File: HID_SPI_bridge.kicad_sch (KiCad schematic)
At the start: 10 parts, among them P1 USB_C_Plug_USB2.0, U1 STM32F042K4Tx

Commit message: [ADD](General) v1
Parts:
- added D2: D_Schottky, symbol Device:D_Schottky
- renumbered C6 to C122, C7 to C123, C5 to C124, C8 to C125, C4 to C126, C9 to C127, U1 to U2
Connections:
- net GND: no longer P1.S1 (SHIELD)
- net VBUS: now also D2.1 (K); no longer P1.A4 (VBUS), P1.A9 (VBUS), P1.B4 (VBUS), P1.B9 (VBUS)
- net NRST: now reaches C124.2, U2.4 (NRST)
- net CC: now reaches P1.A5 (CC), R10.2
- net SPI_SCK: now reaches U2.11 (PA5)
- net SPI_MISO: now reaches U2.12 (PA6)
- net SPI_MOSI: now reaches U2.13 (PA7)
- net USB-: now reaches P1.A7 (D-), U2.21 (PA11)
- net USB+: now reaches P1.A6 (D+), U2.22 (PA12)
- net SPI_CS: now reaches U2.6 (PA0)
- new net: D2.2 (A), P1.A4 (VBUS), P1.A9 (VBUS), P1.B4 (VBUS), P1.B9 (VBUS)
- no-connect marks 1 -> 20
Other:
- note added: "Microcontroller for USB interface"
- note added: "USB 2.0"
- company: (none) -> Ryzzen
- title: (none) -> TMR based triple USB Keyboard
- moved on the sheet: C124, P1, R10

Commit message: [ADD](General) v2 split
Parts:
- removed D2: D_Schottky, symbol Device:D_Schottky
- removed P1: USB_C_Plug_USB2.0, symbol Connector:USB_C_Plug_USB2.0
- removed R10: 5.1k, symbol Device:R
- added D38: D_Schottky, symbol Device:D_Schottky
- added J5: USB_C_Receptacle_USB2.0_14P, symbol Connector:USB_C_Receptacle_USB2.0_14P
- added R12, R13: 5.1k, symbol Device:R
- renumbered C122 to C14, C123 to C15, C124 to C16, C125 to C17, C126 to C18, C127 to C19
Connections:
- net GND: now also J5.A1 (GND), J5.A12 (GND), J5.B1 (GND), J5.B12 (GND), R12.1, R13.1
- net USB+: now also U2.21 (PA11), J5.A6 (D+), J5.B6 (D+); no longer U2.22 (PA12)
- net USB-: now also U2.22 (PA12), J5.A7 (D-), J5.B7 (D-); no longer U2.21 (PA11)
- net VBUS: now also D38.1 (K)
- new net: J5.B5 (CC2), R12.2
- new net: D38.2 (A), J5.A4 (VBUS), J5.A9 (VBUS), J5.B4 (VBUS), J5.B9 (VBUS)
- new net: J5.A5 (CC1), R13.2
- no-connect marks 20 -> 19

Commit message: [FIX](General) footprints
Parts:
- renumbered D38 to D3, R12 to R7, R13 to R8, U2 to U3

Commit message: [ADD](General) added all footprints expect leds
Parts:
- C14, C15, C16, C17, C18, C19: footprint (none) -> Capacitor_SMD:C_0603_1608Metric_Pad1.08x0.95mm_HandSolder
- R7, R8: footprint (none) -> Resistor_SMD:R_0603_1608Metric_Pad0.98x0.95mm_HandSolder
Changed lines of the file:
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@@
 			)
 		)
-		(property "Footprint" ""
+		(property "Footprint" "Capacitor_SMD:C_0603_1608Metric_Pad1.08x0.95mm_HandSolder"
 			(at 98.7552 68.58 0)
 			(effects
@@
 			)
 		)
-		(property "Footprint" ""
+		(property "Footprint" "Capacitor_SMD:C_0603_1608Metric_Pad1.08x0.95mm_HandSolder"
 			(at 106.68 76.5048 0)
 			(effects
@@
 			)
 		)
-		(property "Footprint" ""
+		(property "Footprint" "Capacitor_SMD:C_0603_1608Metric_Pad1.08x0.95mm_HandSolder"
 			(at 111.4552 68.58 0)
 			(effects
@@
 			)
 		)
-		(property "Footprint" ""
+		(property "Footprint" "Resistor_SMD:R_0603_1608Metric_Pad0.98x0.95mm_HandSolder"
 			(at 195.58 109.728 90)
 			(effects
@@
 			)
 		)
-		(property "Footprint" ""
+		(property "Footprint" "Capacitor_SMD:C_0603_1608Metric_Pad1.08x0.95mm_HandSolder"
 			(at 131.7752 66.04 0)
 			(effects
@@
 			)
 		)
-		(property "Footprint" ""
+		(property "Footprint" "Capacitor_SMD:C_0603_1608Metric_Pad1.08x0.95mm_HandSolder"
 			(at 86.0552 68.58 0)
 			(effects
@@
 			)
 		)
-		(property "Footprint" ""
+		(property "Footprint" "Capacitor_SMD:C_0603_1608Metric_Pad1.08x0.95mm_HandSolder"
 			(at 153.3652 66.04 0)
 			(effects
@@
 			)
 		)
-		(property "Footprint" ""
+		(property "Footprint" "Resistor_SMD:R_0603_1608Metric_Pad0.98x0.95mm_HandSolder"
 			(at 195.58 112.268 90)
 			(effects

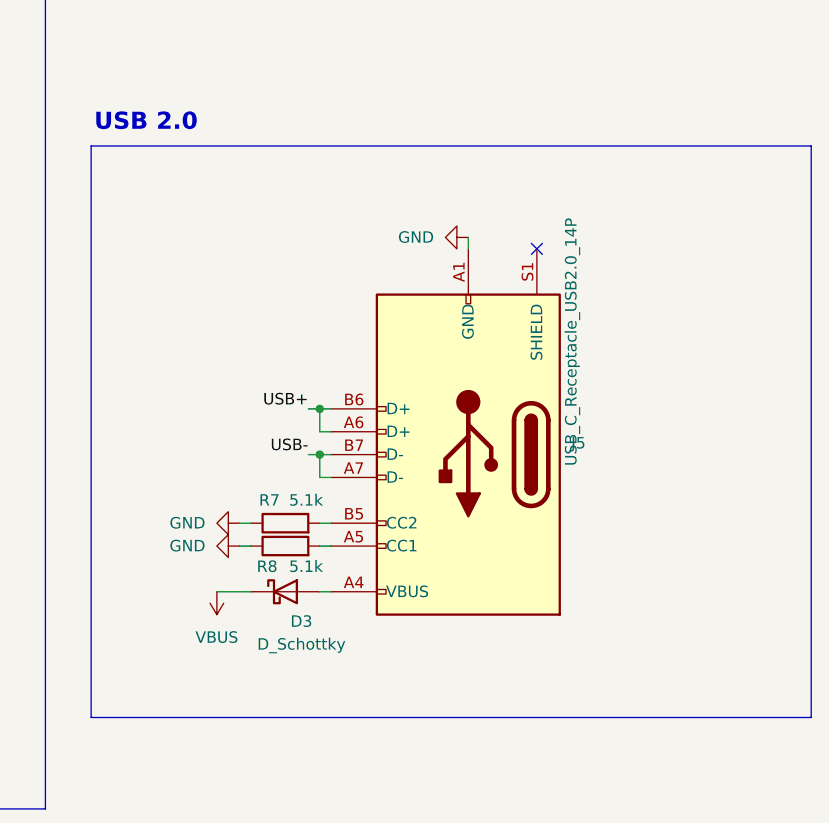
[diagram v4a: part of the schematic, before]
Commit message: [ADD](General) added all footprints
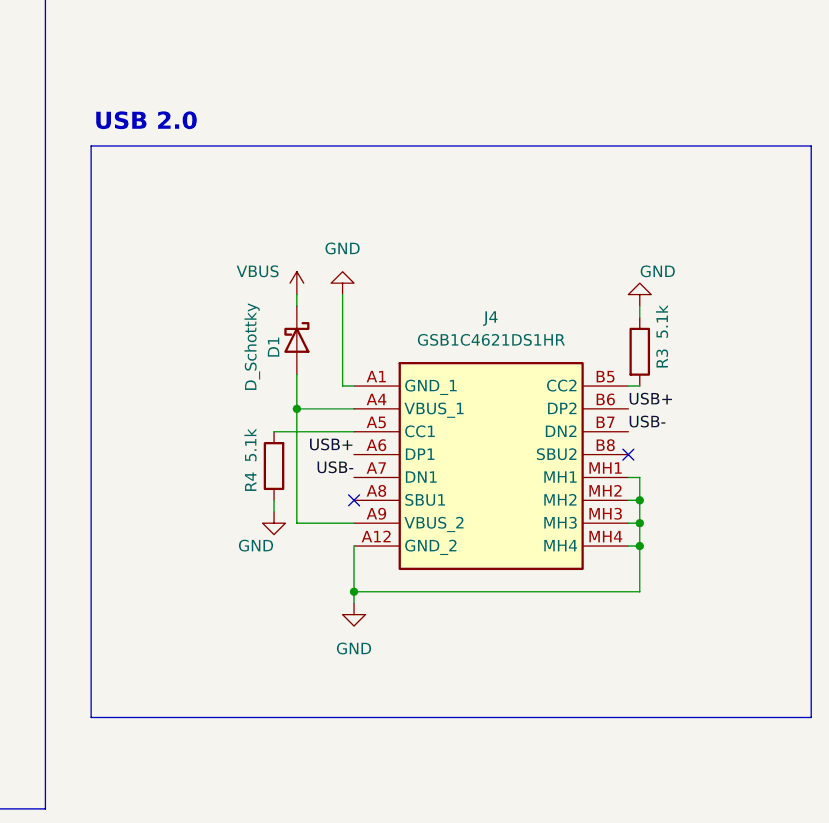
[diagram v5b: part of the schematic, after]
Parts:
- removed D3: D_Schottky, symbol Device:D_Schottky
- removed J5: USB_C_Receptacle_USB2.0_14P, symbol Connector:USB_C_Receptacle_USB2.0_14P
- removed R7, R8: 5.1k, Resistor_SMD:R_0603_1608Metric_Pad0.98x0.95mm_HandSolder, symbol Device:R
- added D1: D_Schottky, CUHS20S30:CUHS20S40H3F, symbol Device:D_Schottky
- added J4: GSB1C4621DS1HR, GSB1C4621DS1HR:GSB1C4621DS1HR, symbol GSB1C4621DS1HR:GSB1C4621DS1HR
- added R3, R4: 5.1k, Resistor_SMD:R_0603_1608Metric_Pad0.98x0.95mm_HandSolder, symbol Device:R
- FB2: footprint (none) -> BLM21PG121SN1D:BLM21AG102BH1J
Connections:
- net GND: now also J4.A1 (GND_1), J4.A12 (GND_2), J4.MH1, J4.MH2, J4.MH3, J4.MH4, R3.1, R4.1
- net USB+: now also J4.A6 (DP1), J4.B6 (DP2)
- net USB-: now also J4.A7 (DN1), J4.B7 (DN2)
- net VBUS: now also D1.1 (K)
- new net: D1.2 (A), J4.A4 (VBUS_1), J4.A9 (VBUS_2)
- new net: J4.B5 (CC2), R3.2
- new net: J4.A5 (CC1), R4.2
- no-connect marks 19 -> 20

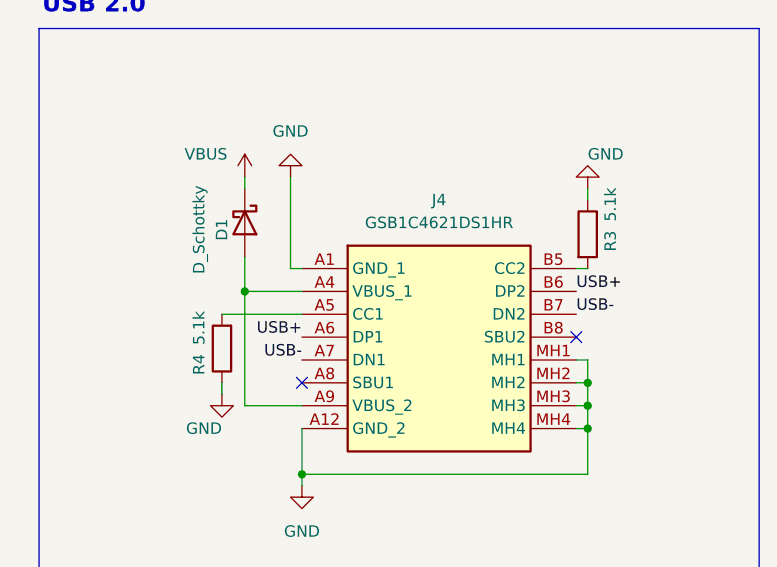
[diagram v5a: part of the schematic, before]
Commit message: [FIX](USB) main usb net labels
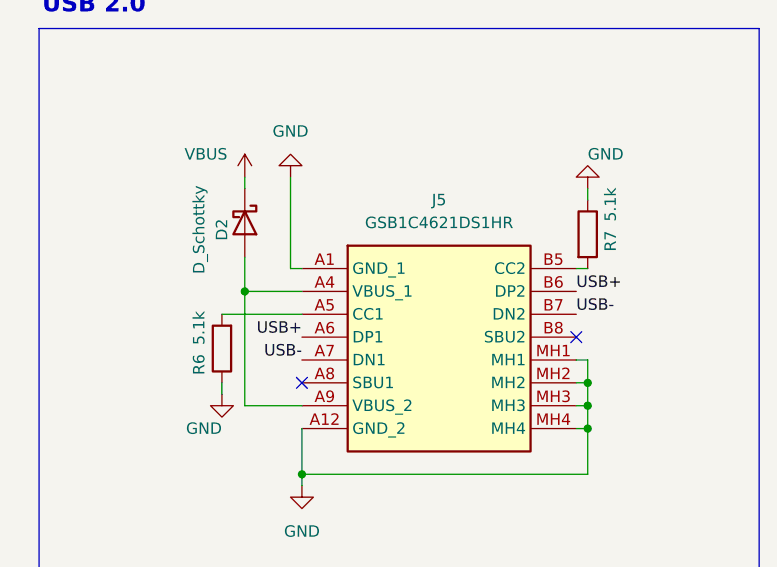
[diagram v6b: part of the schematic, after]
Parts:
- renumbered D1 to D2, J4 to J5, R4 to R6, R3 to R7

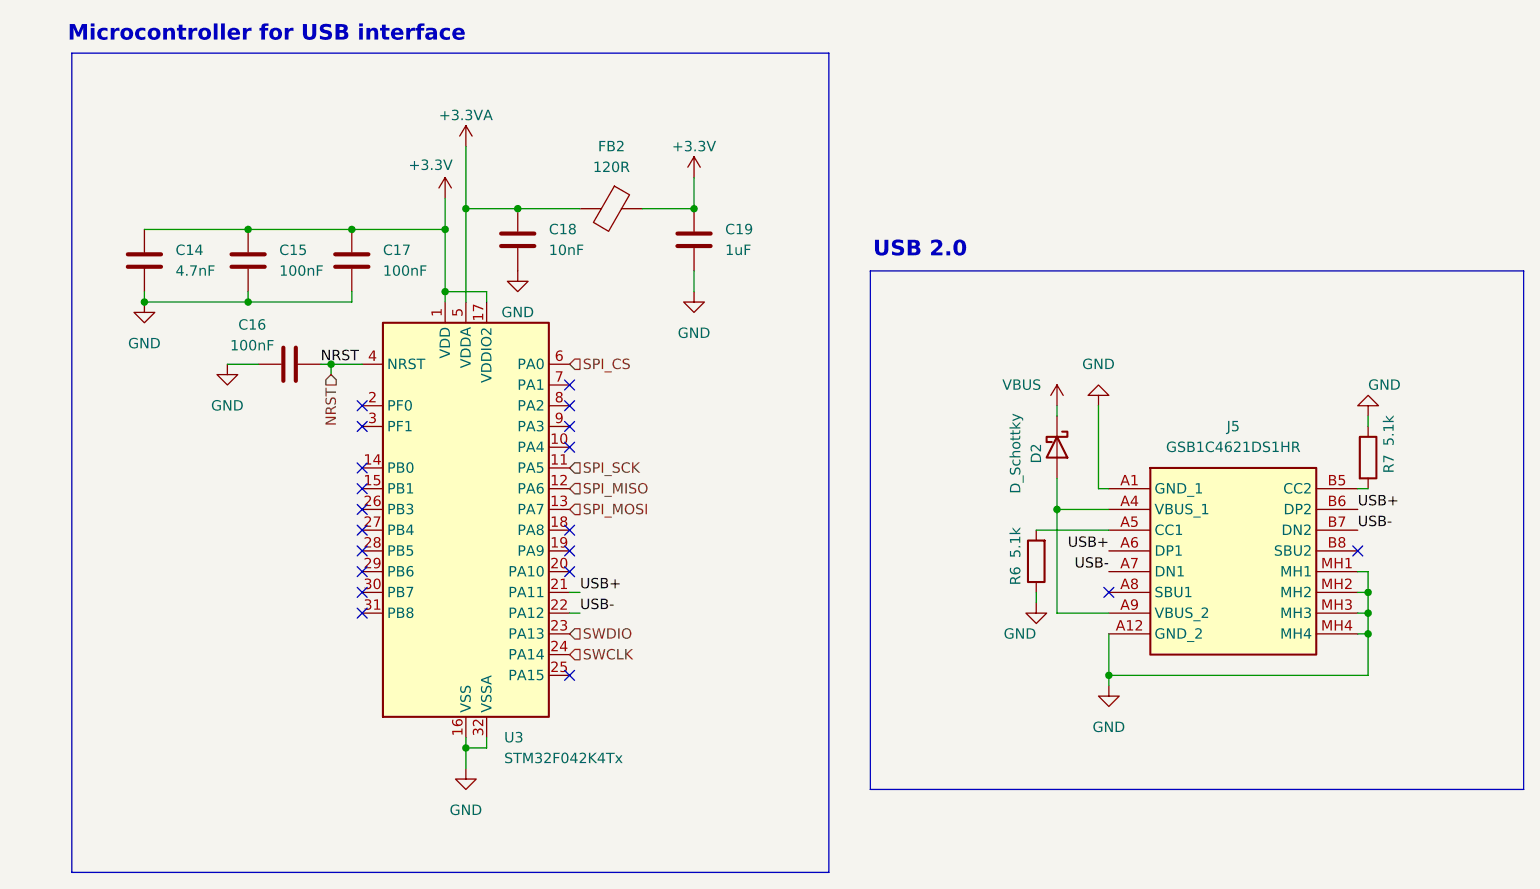
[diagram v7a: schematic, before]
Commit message: [ADD](PCB) led and tmr caps placement
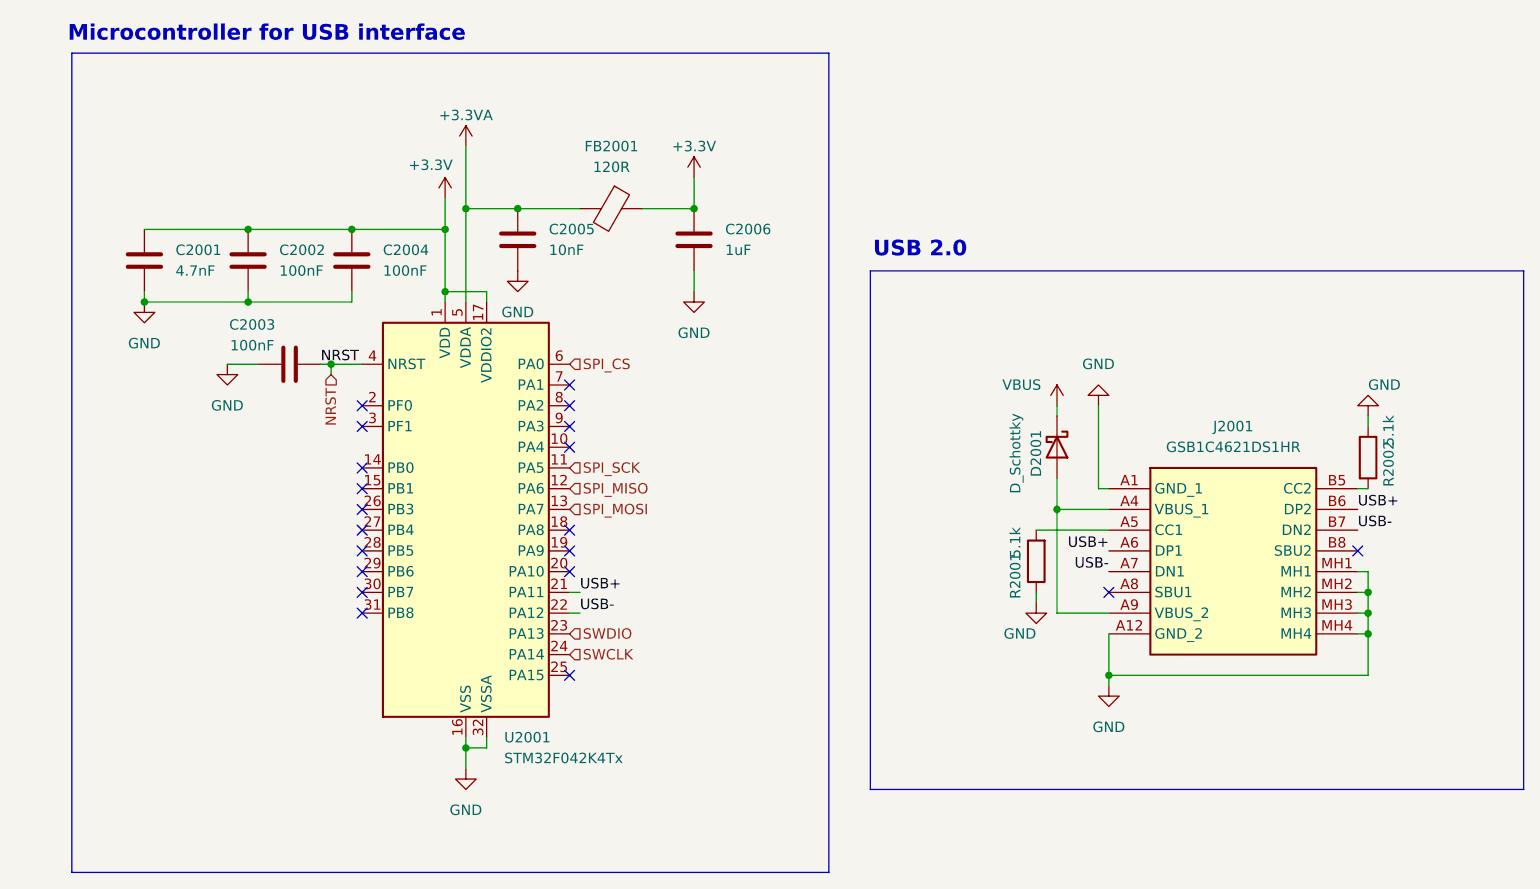
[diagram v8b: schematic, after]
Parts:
- renumbered C14 to C2001, C15 to C2002, C16 to C2003, C17 to C2004, C18 to C2005, C19 to C2006, D2 to D2001, FB2 to FB2001, J5 to J2001, R6 to R2001, R7 to R2002, U3 to U2001
